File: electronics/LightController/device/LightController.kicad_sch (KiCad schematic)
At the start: 8 parts, among them J1 RF_TX, J2 AC, SW1 RotaryEncoder_Switch, U1 ATMEGA328P-AU

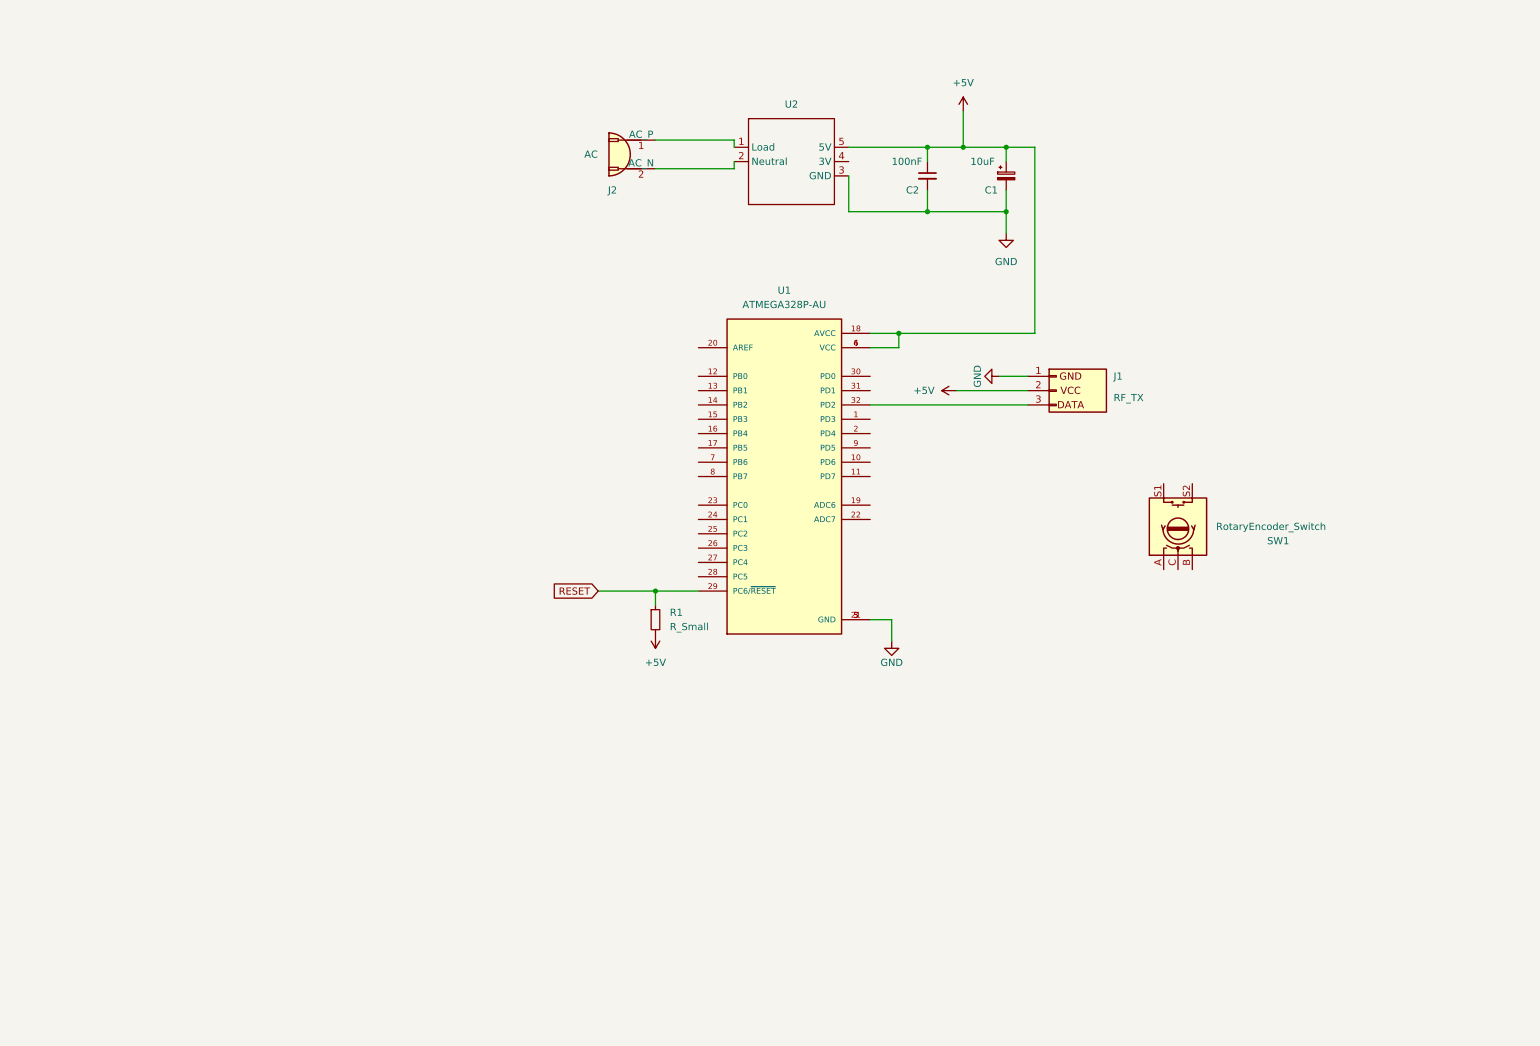
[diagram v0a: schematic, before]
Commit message: Improve file naming & Design V2 Dimmer iteration & Lay components in PCB
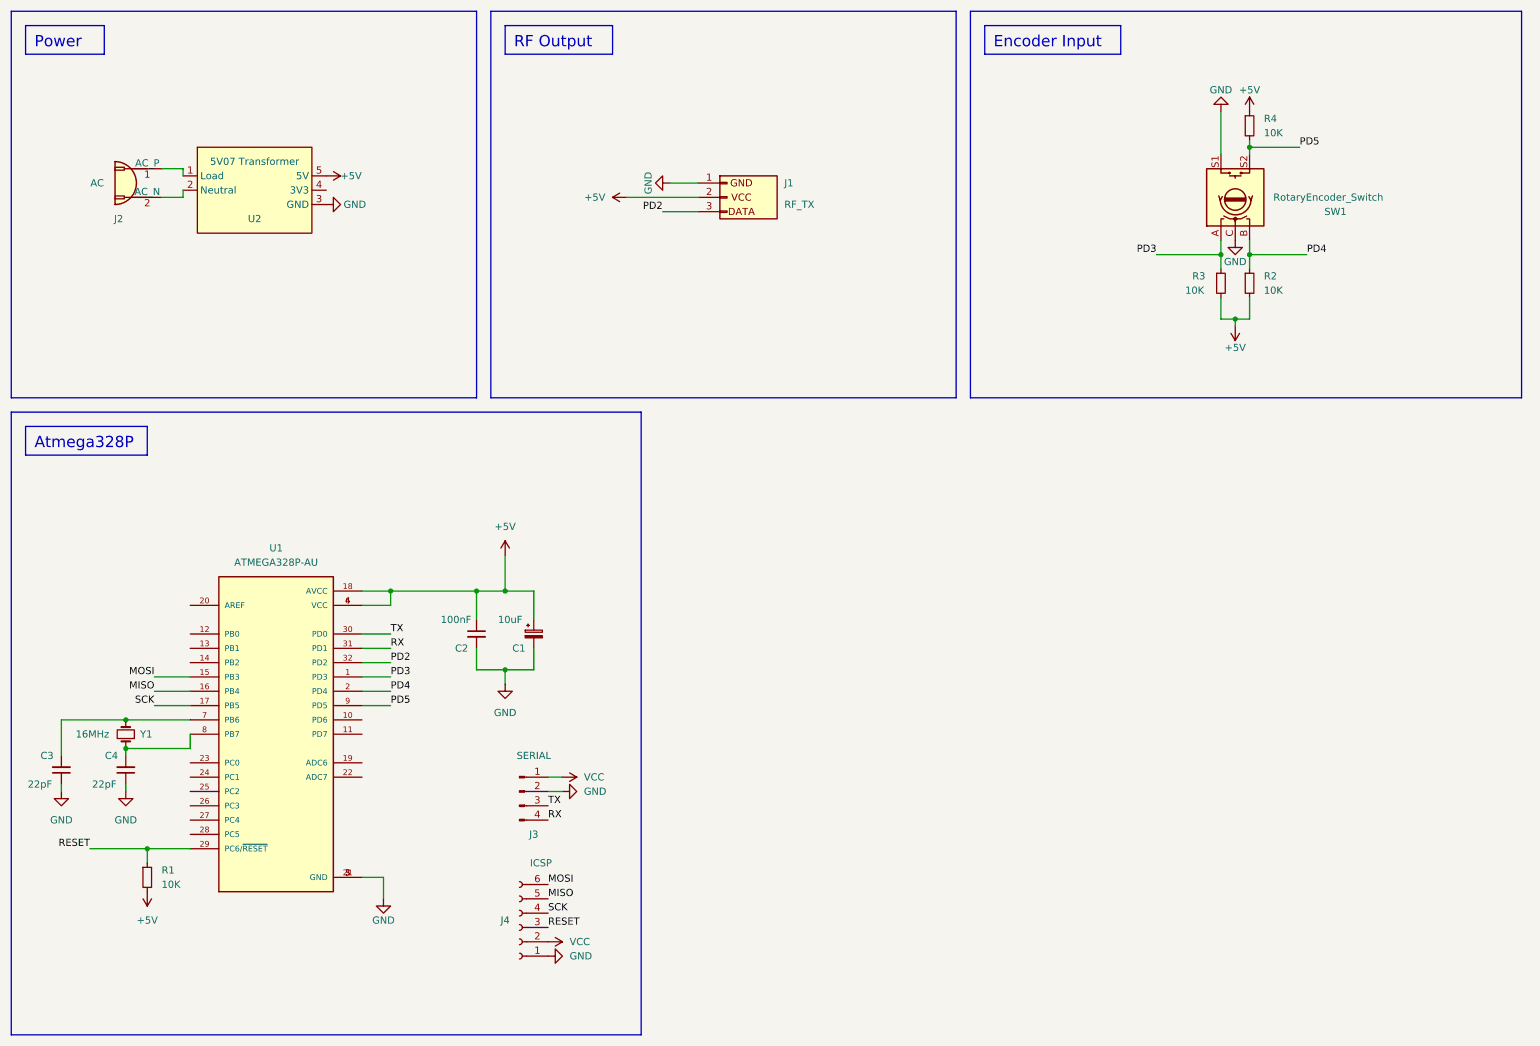
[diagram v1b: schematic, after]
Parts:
- added C3, C4: 22pF, Capacitor_SMD:C_0805_2012Metric_Pad1.18x1.45mm_HandSolder, symbol Device:C_Small
- added J3: SERIAL, Connector_PinHeader_2.54mm:PinHeader_1x04_P2.54mm_Vertical, symbol Connector:Conn_01x04_Pin
- added J4: ICSP, Connector_JST:JST_PH_B6B-PH-K_1x06_P2.00mm_Vertical, symbol Connector:Conn_01x06_Socket
- added R2, R3, R4: 10K, Resistor_SMD:R_1206_3216Metric_Pad1.30x1.75mm_HandSolder, symbol Device:R_Small
- added Y1: 16MHz, Crystal:Crystal_HC49-4H_Vertical, symbol Device:Crystal_Small
- C1: footprint (none) -> Capacitor_SMD:CP_Elec_6.3x4.9
- C2: footprint (none) -> Capacitor_SMD:C_1210_3225Metric_Pad1.33x2.70mm_HandSolder
- J1: footprint (none) -> AA_Footprints:RF ASK Emitter
- J2: footprint (none) -> AA_Footprints:Terminal_KF128-2P
- R1: value R_Small -> 10K; footprint (none) -> Resistor_SMD:R_1206_3216Metric_Pad1.30x1.75mm_HandSolder
- SW1: footprint (none) -> AA_Footprints:RotaryEncoder_Alps_EC11E-Switch_Vertical_H20mm
- U1: footprint QFP80P900X900X120-32N -> AA_Footprints:Atmega328p-TQFP
- U2: value ~ -> 5V07 Transformer; footprint (none) -> AA_Footprints:5V07
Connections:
- net +5V: now also R2.2, R3.2, R4.1
- net GND: now also SW1.C, SW1.S1, C3.1, C4.1, J3.2 (Pin_2), J4.1 (Pin_1)
- net RESET: now also J4.3 (Pin_3)
- net PD3: now reaches SW1.A
- net PD3: now also U1.1 (PD3), R3.1
- net PD4: now reaches SW1.B
- net PD4: now also U1.2 (PD4), R2.1
- net PD5: now reaches SW1.S2
- net PD5: now also U1.9 (PD5), R4.2
- net MOSI: now reaches U1.15 (PB3)
- net MOSI: now also J4.6 (Pin_6)
- net MISO: now reaches U1.16 (PB4)
- net MISO: now also J4.5 (Pin_5)
- net SCK: now reaches U1.17 (PB5)
- net SCK: now also J4.4 (Pin_4)
- net TX: now reaches U1.30 (PD0)
- net TX: now also J3.3 (Pin_3)
- net RX: now reaches U1.31 (PD1)
- net RX: now also J3.4 (Pin_4)
- net PD2: now reaches J1.3 (DATA), U1.32 (PD2)
- net at U1.7 (PB6): now also C3.2, Y1.2
- net at U1.8 (PB7): now also C4.2, Y1.1
- new net VCC: J3.1 (Pin_1), J4.2 (Pin_2)
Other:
- company: (none) -> Pablo Ortiz López
- title: (none) -> LightController
- moved on the sheet: C1, C2, J1, J2, R1, SW1, U1

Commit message: Finish LightController PCB design with 3 switches
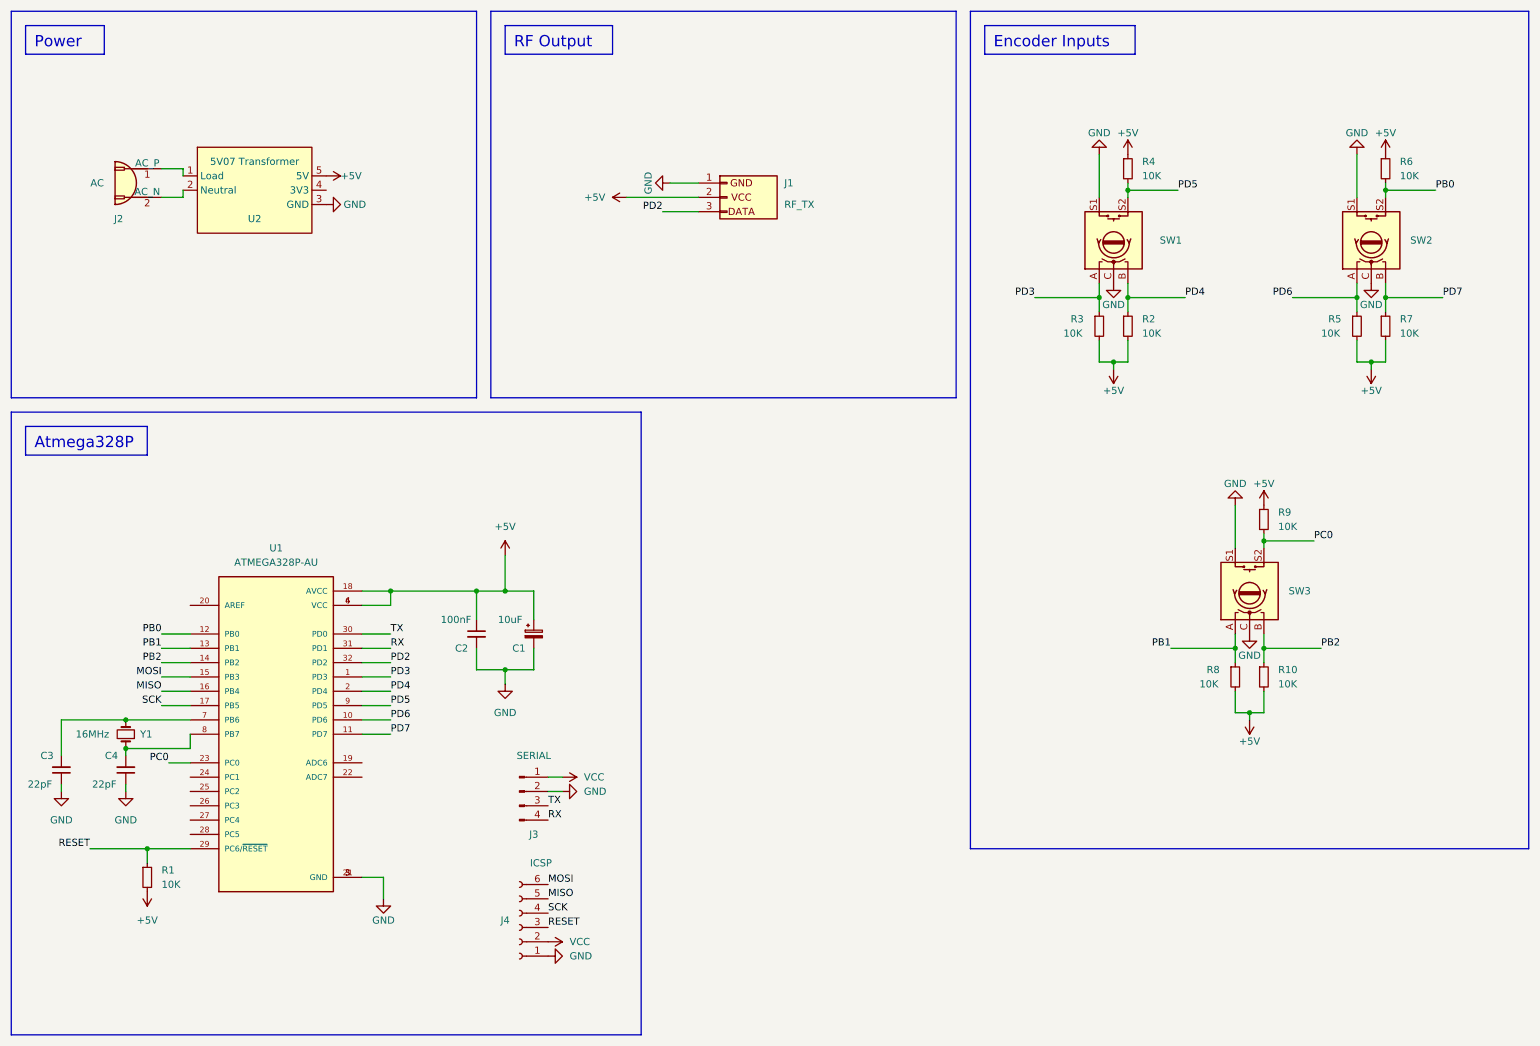
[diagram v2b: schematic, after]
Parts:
- added R10, R5, R6, R7, R8, R9: 10K, Resistor_SMD:R_1206_3216Metric_Pad1.30x1.75mm_HandSolder, symbol Device:R_Small
- added SW2, SW3: RotaryEncoder_Switch, AA_Footprints:RotaryEncoder_Alps_EC11E-Switch_Vertical_H20mm, symbol Device:RotaryEncoder_Switch
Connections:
- net +5V: now also R10.2, R5.2, R6.1, R7.2, R8.2, R9.1
- net GND: now also SW2.C, SW2.S1, SW3.C, SW3.S1
- net PD6: now reaches U1.10 (PD6)
- net PD6: now also R5.1, SW2.A
- net PD7: now reaches U1.11 (PD7)
- net PD7: now also R7.1, SW2.B
- net PB0: now reaches U1.12 (PB0)
- net PB0: now also R6.2, SW2.S2
- net PB1: now reaches U1.13 (PB1)
- net PB1: now also R8.1, SW3.A
- net PB2: now reaches U1.14 (PB2)
- net PB2: now also R10.1, SW3.B
- net PC0: now reaches U1.23 (PC0)
- net PC0: now also R9.2, SW3.S2
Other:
- moved on the sheet: R2, R3, R4, SW1
